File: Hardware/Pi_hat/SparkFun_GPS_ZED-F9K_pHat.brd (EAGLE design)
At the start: 65 x 56.5 mm, 41 parts, among them J2 RASPBERRYPI-40-PIN-GPIO_PTH_N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, J4 U.FL, U1 UBLOX_ZED_F9K, U3 TRIPLE_BUFFER_74LVC3G07

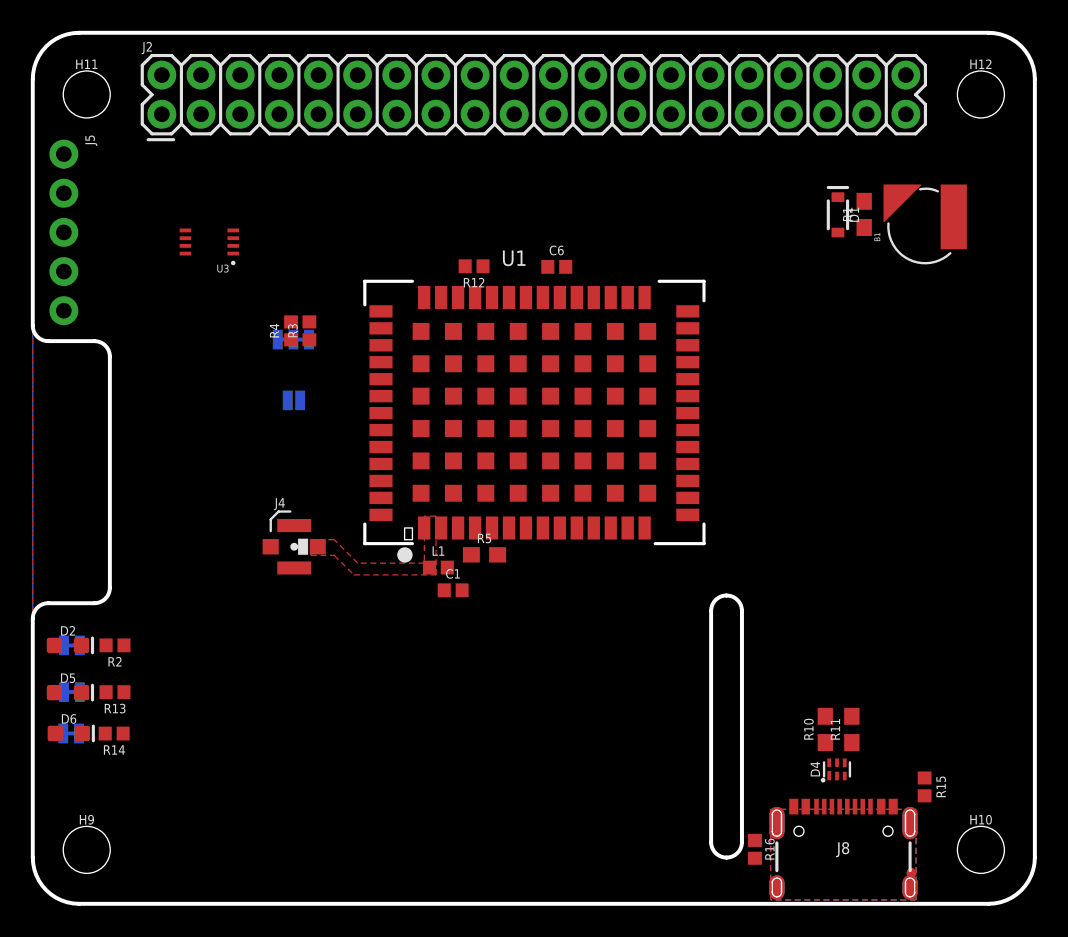
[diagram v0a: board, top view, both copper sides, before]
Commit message: Add prelimnary trace routing
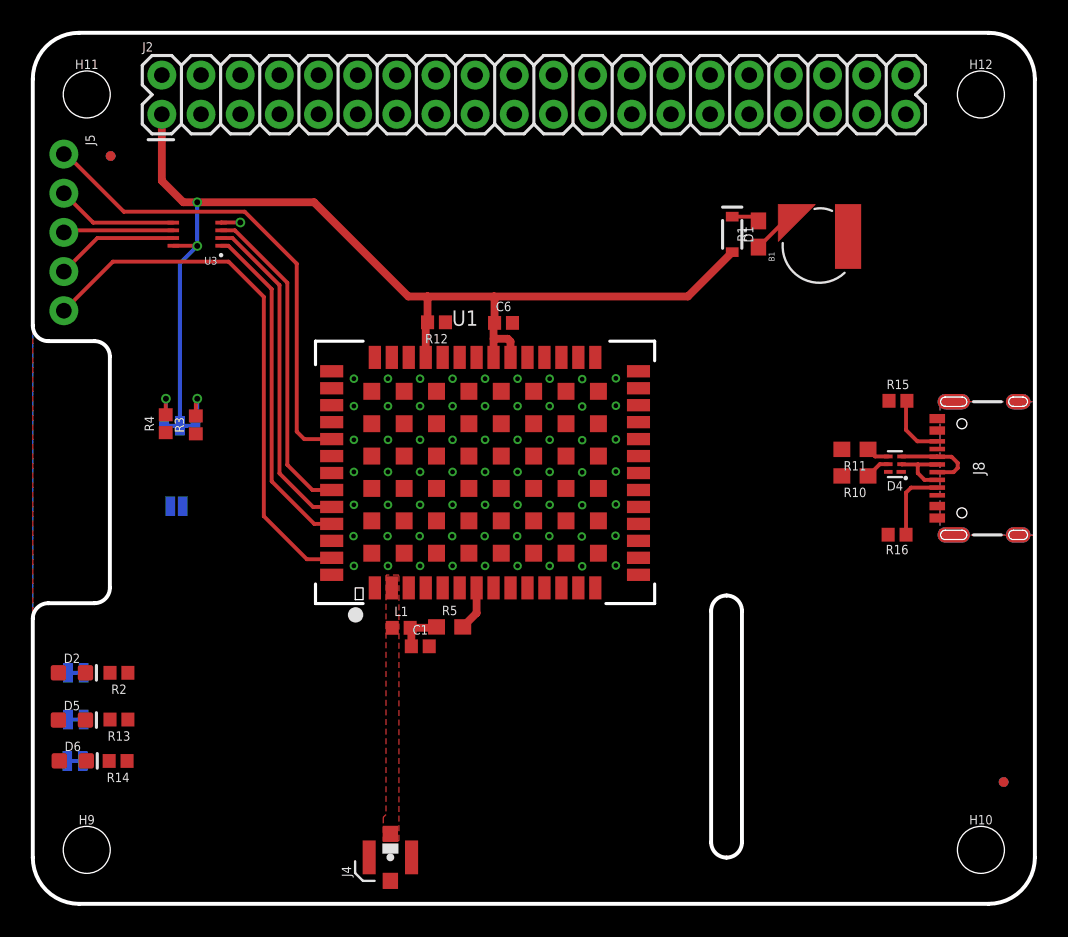
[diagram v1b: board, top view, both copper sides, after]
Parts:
- moved R15 25.1 mm to (56.1, 32.6), turned to 0 degrees
- moved J8 23.0 mm to (58.8, 28.2), turned to 90 degrees
- moved R16 22.4 mm to (56.1, 23.9), turned to 0 degrees
- moved J4 21.1 mm to (23.2, 3.01), turned to 90 degrees
- moved D4 20.2 mm to (55.9, 28.5), turned to 180 degrees
- moved R11 18.2 mm to (53.3, 29.5), turned to 180 degrees
- moved R10 16.6 mm to (53.3, 27.8), turned to 180 degrees
- moved JP1 10.3 mm to (9.32, 25.8)
- moved R4 10.1 mm to (8.62, 31.1)
- moved R3 9.56 mm to (10.6, 31.1)
- moved JP2 9.25 mm to (9.54, 31.0)
- moved FD10 8.40 mm to (63.0, 7.90), turned to 270 degrees
- moved FD9 8.40 mm to (63.0, 7.90), turned to 90 degrees
- moved R1 6.97 mm to (47.1, 43.4)
- moved B1 6.97 mm to (51.0, 42.7)
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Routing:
- net 3.3V: track 0.00 -> 72.3 mm, vias 0 -> 2
- net PPS: track 0.00 -> 35.1 mm
- net TX_READY: track 0.00 -> 31.4 mm
- net INT_IN: track 0.00 -> 22.0 mm
- net !SAFEBOOT_OUT: track 0.00 -> 21.6 mm
- net !RESET_IN: track 0.00 -> 21.1 mm
- net !RESET_OUT: track 0.00 -> 8.00 mm
- net INT_OUT: track 0.00 -> 7.89 mm
- net !SAFEBOOT_IN: track 0.00 -> 7.16 mm
- net USB_D+: track 0.00 -> 5.58 mm
- net N$18: track 0.00 -> 4.89 mm
- net USB_D-: track 0.00 -> 4.33 mm
- net N$12: track 0.00 -> 4.25 mm
- net N$5: track 0.00 -> 2.97 mm
- net N$1: track 0.00 -> 2.96 mm, vias 0 -> 1
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
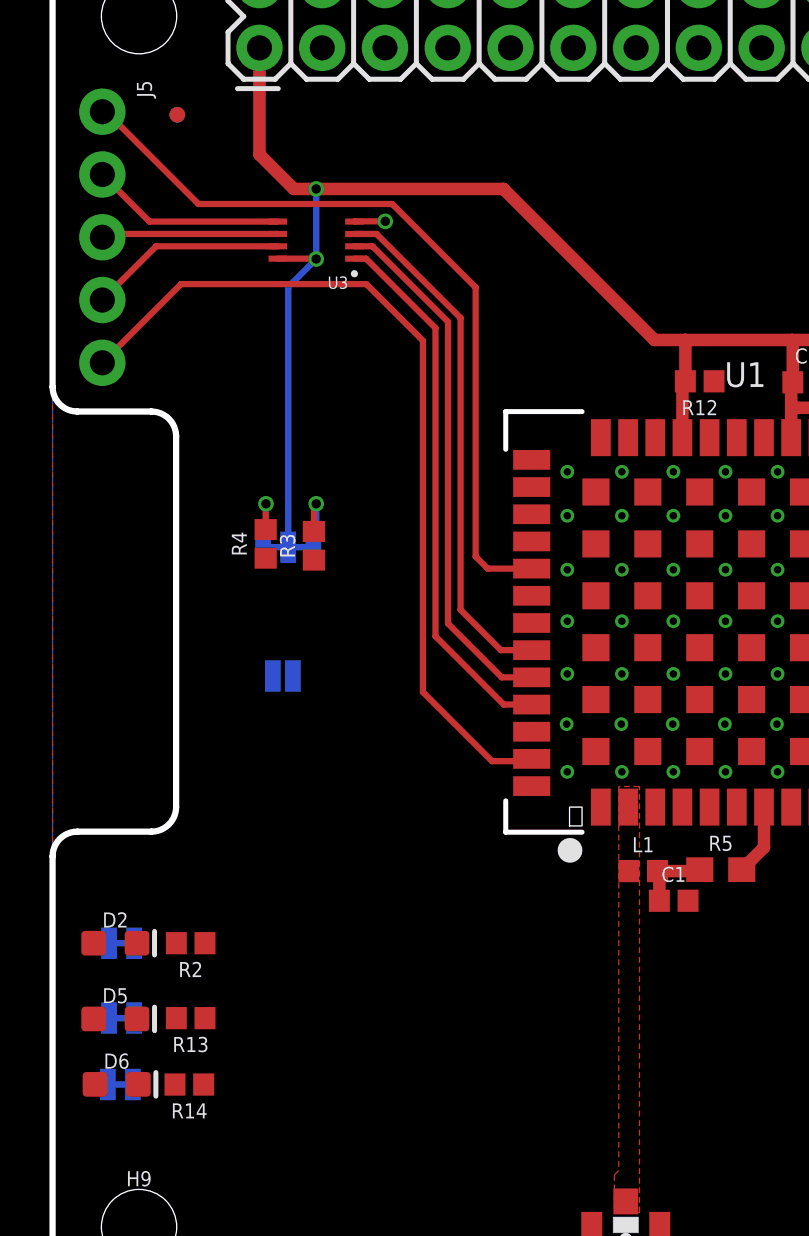
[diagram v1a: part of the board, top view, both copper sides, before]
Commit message: Adds nets for data lines
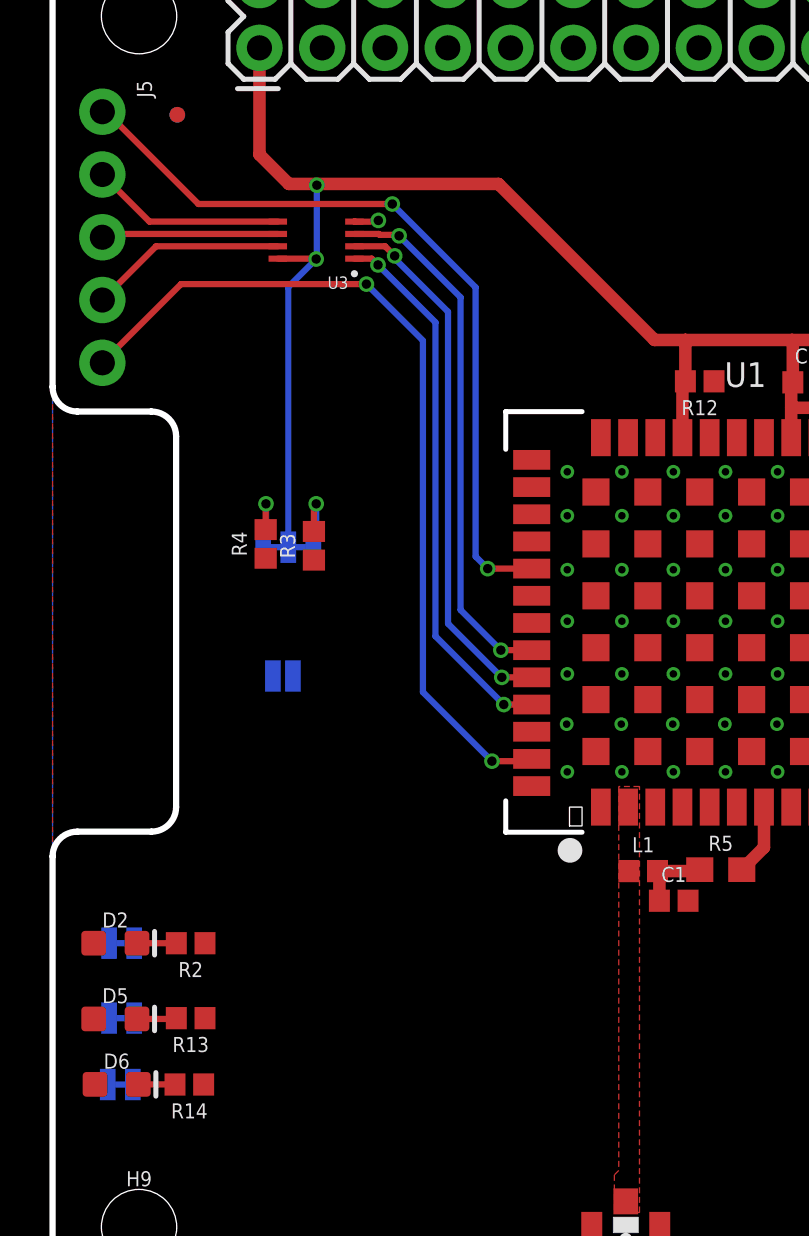
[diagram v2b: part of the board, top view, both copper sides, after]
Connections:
- net RXI/MOSI: now also J2.10, J2.19
- net SCL/CLK: now also J2.23, J2.5
- net SDA/!CS: now also J2.24, J2.3
- net TXO/MISO: now also J2.21, J2.8
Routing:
- net N$24: track 0.00 -> 1.60 mm
- net N$4: track 0.00 -> 1.59 mm
- net N$25: track 0.00 -> 1.49 mm
- net !RESET_IN: track 21.1 -> 21.6 mm, vias 0 -> 2
- net !SAFEBOOT_OUT: track 21.6 -> 21.9 mm, vias 0 -> 2
- net INT_IN: track 22.0 -> 22.1 mm, vias 0 -> 2
- net TX_READY: vias 0 -> 2
- net PPS: vias 0 -> 2

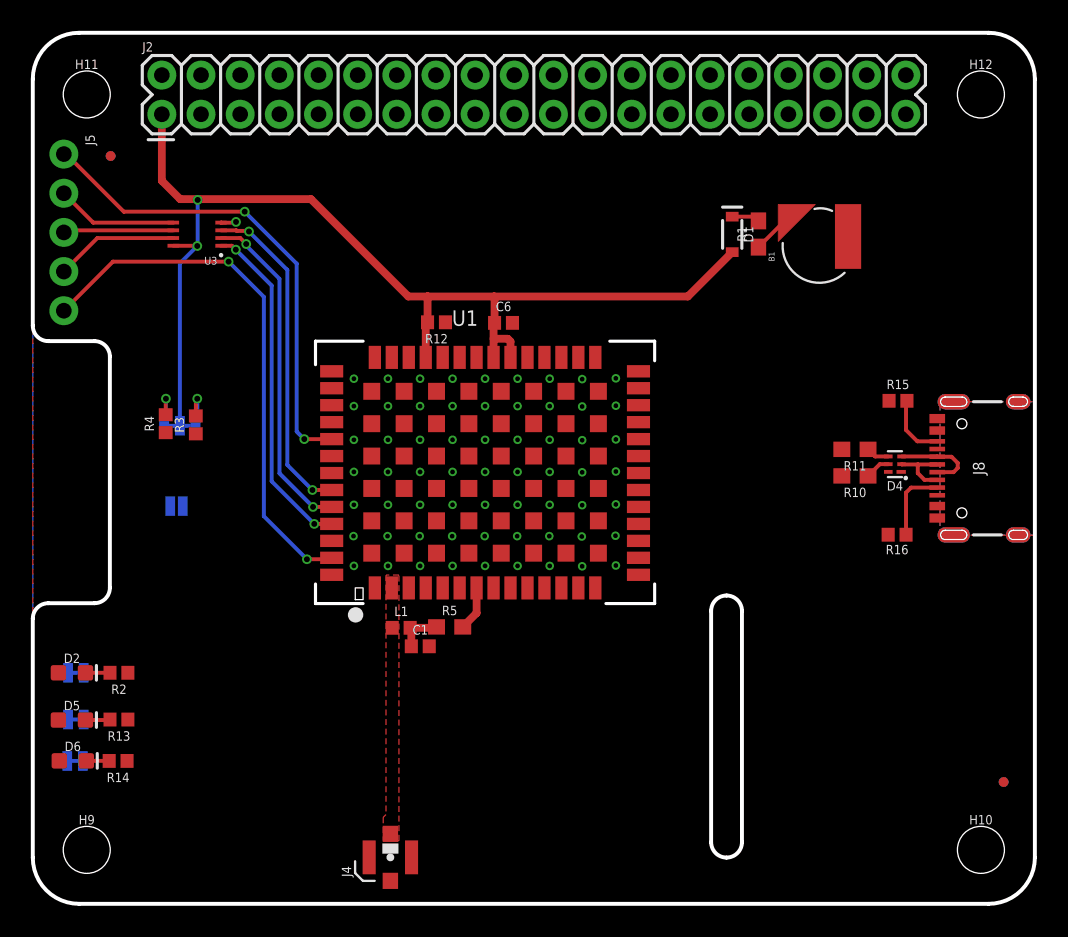
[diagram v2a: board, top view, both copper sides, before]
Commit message: Finishes pi hat design and adds some labels
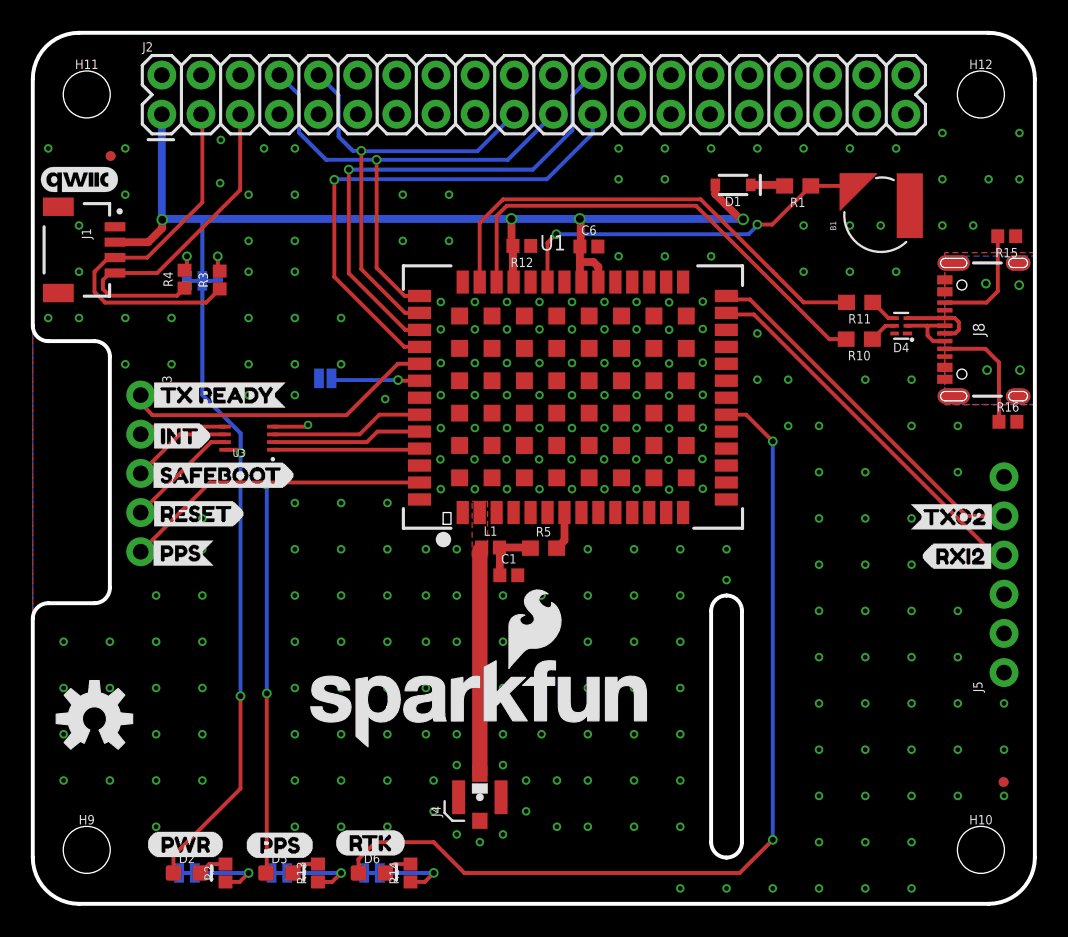
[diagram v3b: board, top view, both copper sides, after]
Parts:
- added J1: QWIIC_RIGHT_ANGLE, SparkFun-Connectors:JST04_1MM_RA
- added J3: (no value), SparkFun-Connectors:1X05_NO_SILK
- added LOGO1: SFE_LOGO_NAME_FLAME.2_INCH, SparkFun-Aesthetics:SFE_LOGO_NAME_FLAME_.2
- added LOGO2: OSHW-LOGOM, SparkFun-Aesthetics:OSHW-LOGO-M
- added LOGO3: QWIIC_LOGO_5MM, SparkFun-Aesthetics:QWIIC_5MM
- added U$1: (no value), ALL_LABELS:INT1
- added U$10: (no value), moar:TXO21
- added U$2: (no value), ALL_LABELS:PPS4
- added U$3: (no value), ALL_LABELS:PPS6
- added U$4: (no value), ALL_LABELS:PWR7
- added U$5: (no value), ALL_LABELS:RTK5
- added U$6: (no value), ALL_LABELS:RXI28
- added U$7: (no value), ALL_LABELS:SAFEBOOT2
- added U$8: (no value), moar:RESET0
- added U$9: (no value), ALL_LABELS:TX_READY0
- J5: device SparkFun-Connectors:1X05_NO_SILK -> SparkFun-Connectors:1X06_NO_SILK
- moved J5 69.6 mm to (63.0, 15.0), turned to 90 degrees
- moved D6 20.7 mm to (22.0, 2.00)
- moved RTK 20.6 mm to (22.0, 2.00)
- moved R14 20.3 mm to (24.5, 2.00), turned to 90 degrees
- moved D5 16.7 mm to (16.0, 2.00)
- moved PPS 16.5 mm to (16.0, 2.00)
- moved R13 16.3 mm to (18.5, 2.00), turned to 90 degrees
- moved D2 15.0 mm to (10.0, 2.00)
- moved PWR 14.9 mm to (10.0, 2.00)
- moved R2 14.7 mm to (12.5, 2.00), turned to 90 degrees
- moved R15 12.8 mm to (63.2, 43.3), turned to 180 degrees
- moved JP1 12.7 mm to (19.0, 34.1)
- moved U3 12.6 mm to (14.0, 30.2)
- moved R16 10.3 mm to (63.3, 31.3), turned to 180 degrees
- moved R11 9.54 mm to (53.6, 39.0)
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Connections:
- removed net VIN: D4.6
- removed net V_USB: D4.1, J8.VBUS1, J8.VBUS2
- new net QWIIC_SCL: J1.4, J2.5, R4.1
- new net QWIIC_SDA: J1.3, J2.3, R3.1
- net !RESET_OUT: now also J3.4; no longer J5.4
- net !SAFEBOOT_IN: now also J3.3; no longer J5.3
- net 3.3V: now also J1.2
- net GND: now also J1.1, J5.1
- net INT_OUT: now also J3.2; no longer J5.2
- net PPS: now also J3.5; no longer J5.5
- net RXI2: now also J5.4
- net SCL/CLK: no longer J2.5, R4.1
- net SDA/!CS: no longer J2.3, R3.1
- net TXO2: now also J5.5
- net TX_READY: now also J3.1; no longer J5.1
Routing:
- net RTK_STAT: track 0.00 -> 59.5 mm, vias 0 -> 2
- net 3.3V: track 72.5 -> 108.7 mm, vias 2 -> 6
- net TXO/MISO: track 0.00 -> 33.3 mm, vias 0 -> 1
- net SCL/CLK: track 0.00 -> 33.0 mm, vias 0 -> 1
- net SDA/!CS: track 0.00 -> 32.5 mm, vias 0 -> 1
- net DPLUS: track 0.00 -> 31.0 mm
- net DMINUS: track 0.00 -> 30.8 mm
- net RXI/MOSI: track 0.00 -> 29.9 mm, vias 0 -> 1
- net QWIIC_SDA: track 0.00 -> 24.7 mm
- net RXI2: track 0.00 -> 24.6 mm
- net TXO2: track 0.00 -> 23.9 mm
- net QWIIC_SCL: track 0.00 -> 22.5 mm
- net V_BATT: track 2.91 -> 23.8 mm, vias 0 -> 2
- net RF_IN: track 0.00 -> 14.5 mm
- net INT_IN: track 22.1 -> 9.55 mm, vias 2 -> 0
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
